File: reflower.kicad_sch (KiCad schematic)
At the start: 37 parts, among them J1 Jack-DC, SW1 RotaryEncoder_Switch, U1 AT32UC3B0256, U2 NCP1117-3.3, U3 MAX31855KASA

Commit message: readme
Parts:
- LOAD1: value (none) -> Conn_01x02; footprint (none) -> Connector_PinHeader_2.54mm:PinHeader_1x06_P2.54mm_Vertical
- SCREEN1: value (none) -> Conn_01x12
- SDCARD1: value (none) -> Conn_01x06
- U4: value (none) -> CPC40055ST; footprint (none) -> OptoDevice:Finder_34.81
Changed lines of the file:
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@@
 (kicad_sch (version 20211123) (generator eeschema)
   (paper "A4")
+  (bus_alias "SPI" (members "SCLK" "MOSI" "MISO"))
   (bus_alias "SCREEN" (members "SC_CS" "BL" "DC" "RES" "T_SDA" "T_SCL" "T_INT"))
-  (bus_alias "SPI" (members "SCLK" "MOSI" "MISO"))
   (junction (at 66.294 144.272) (diameter 0) (color 0 0 0 0)
   )
@@
       (effects (font (size 1.27 1.27)) hide)
     )
-    (property "Value" "" (id 1) (at 173.609 139.192 0))
+    (property "Value" "GND" (id 1) (at 173.609 139.192 0))
     (property "Footprint" "" (id 2) (at 176.784 139.192 0)
       (effects (font (size 1.27 1.27)) hide)
@@
       (effects (font (size 1.27 1.27)) (justify right))
     )
-    (property "Value" "" (id 1) (at 253.365 76.835 0)
+    (property "Value" "Conn_01x12" (id 1) (at 253.365 76.835 0)
       (effects (font (size 1.27 1.27)) (justify right))
     )
@@
       (effects (font (size 1.27 1.27)) (justify right))
     )
-    (property "Value" "" (id 1) (at 253.365 146.05 0)
+    (property "Value" "Conn_01x02" (id 1) (at 253.365 146.05 0)
       (effects (font (size 1.27 1.27)) (justify right))
     )
-    (property "Footprint" "" (id 2) (at 254.635 152.4 0)
+    (property "Footprint" "Connector_PinHeader_2.54mm:PinHeader_1x06_P2.54mm_Vertical" (id 2) (at 254.635 152.4 0)
       (effects (font (size 1.27 1.27)) hide)
     )
@@
     (in_bom yes) (on_board yes)
     (property "Reference" "U4" (id 0) (at 184.404 141.732 0))
-    (property "Value" "" (id 1) (at 184.404 144.272 0))
-    (property "Footprint" "" (id 2) (at 179.324 141.732 0)
+    (property "Value" "CPC40055ST" (id 1) (at 184.404 144.272 0))
+    (property "Footprint" "OptoDevice:Finder_34.81" (id 2) (at 179.324 141.732 0)
       (effects (font (size 1.27 1.27) italic) (justify left) hide)
     )
@@
       (effects (font (size 1.27 1.27)) (justify right))
     )
-    (property "Value" "" (id 1) (at 253.365 117.475 0)
+    (property "Value" "Conn_01x06" (id 1) (at 253.365 117.475 0)
       (effects (font (size 1.27 1.27)) (justify right))
     )

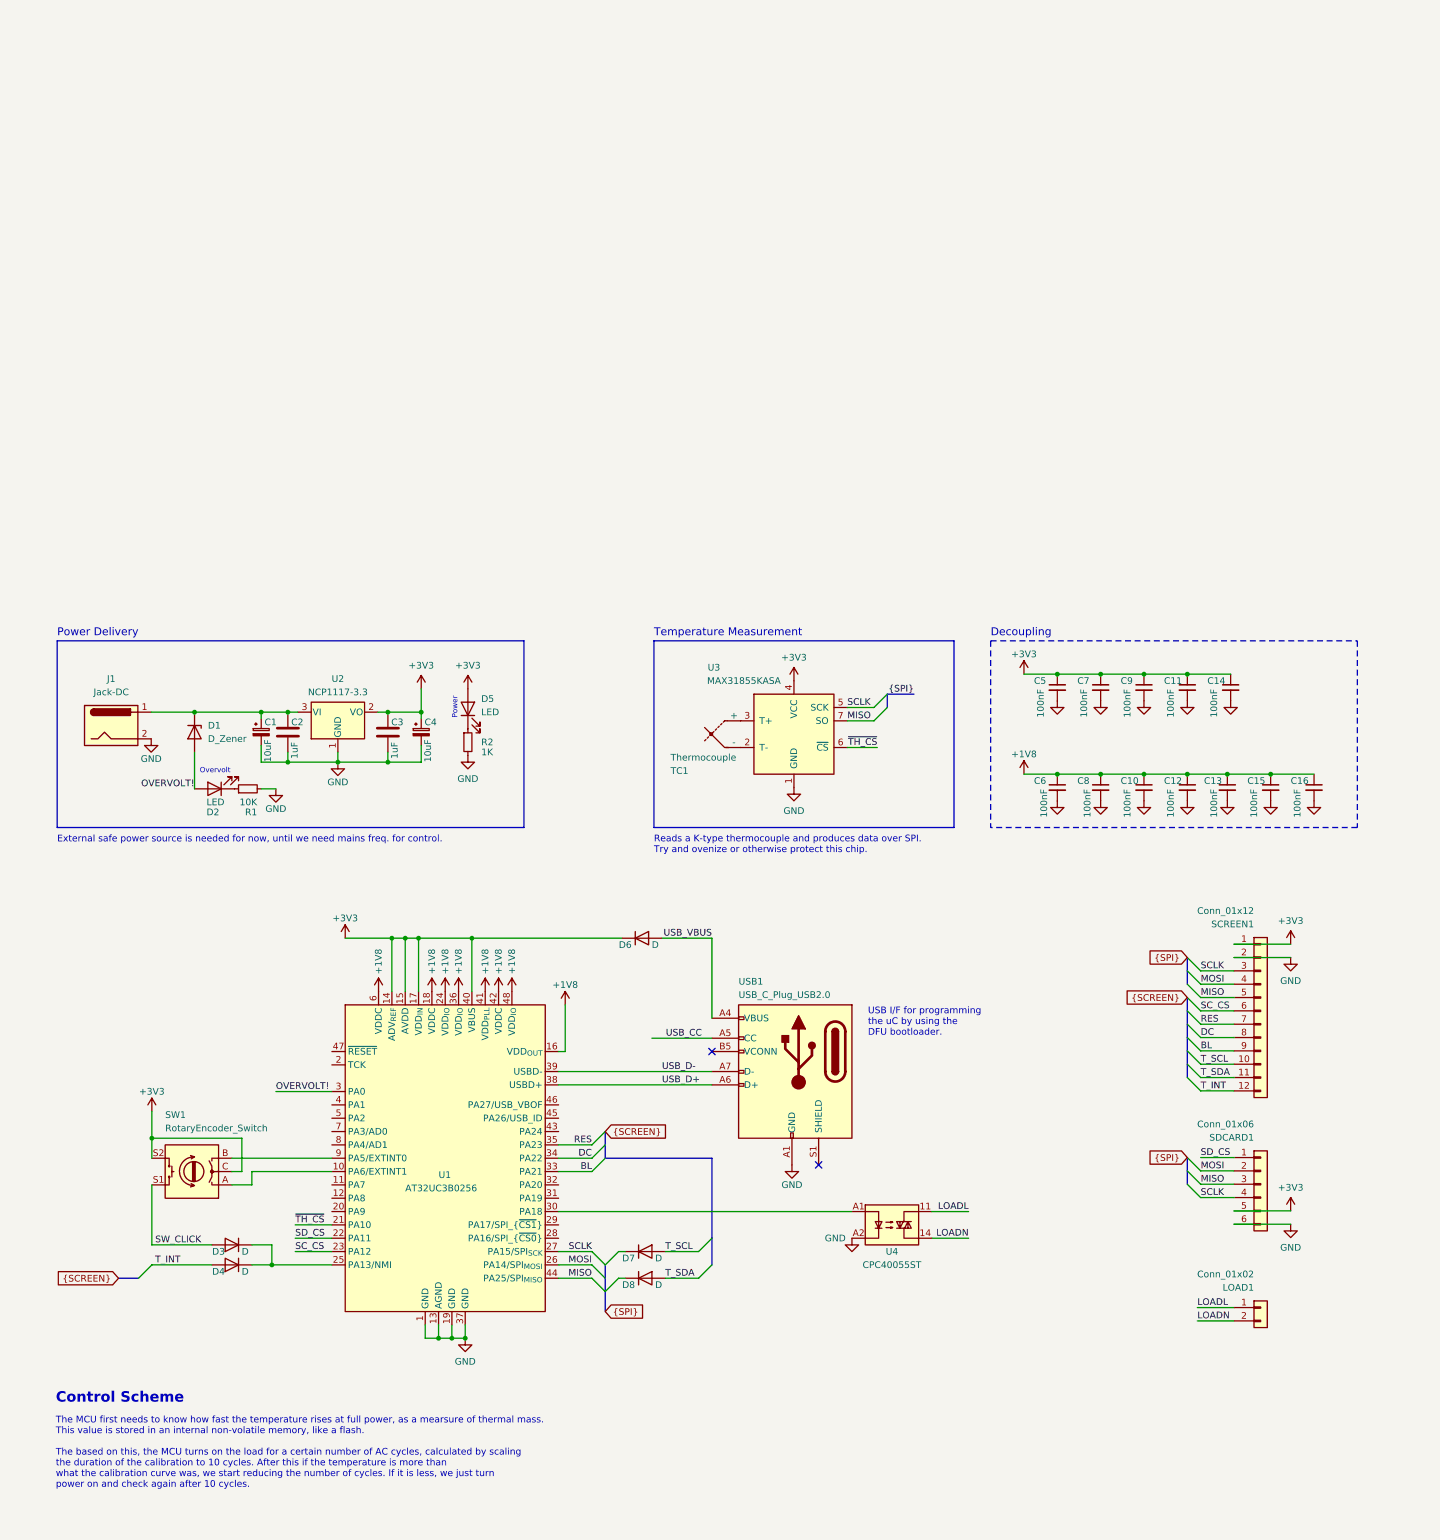
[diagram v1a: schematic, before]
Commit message: added separate SD card slot
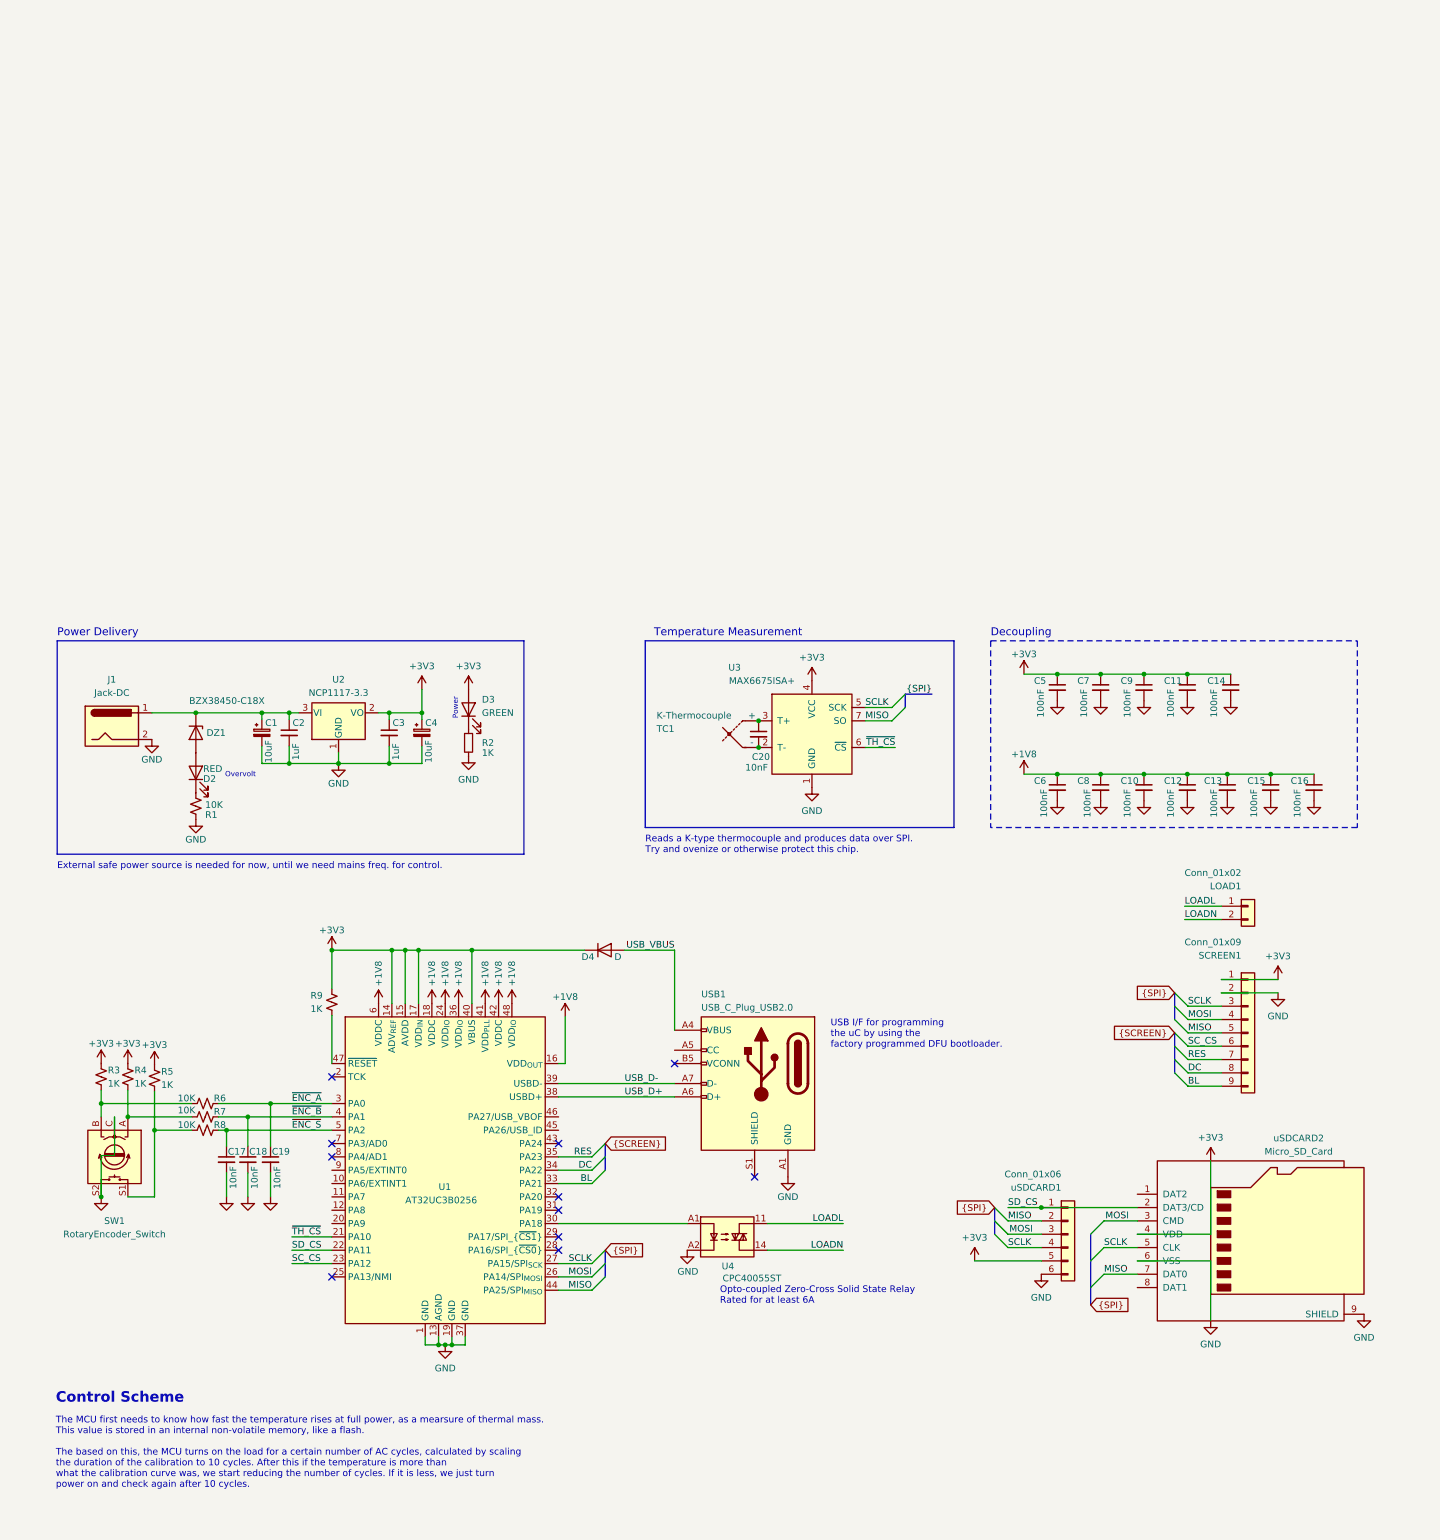
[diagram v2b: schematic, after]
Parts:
- removed D3, D4, D7, D8: D, symbol Device:D
- added C17, C18, C19, C20: 10nF, Capacitor_SMD:C_0603_1608Metric, symbol Device:C_Small
- added R3, R4, R5, R9: 1K, Resistor_SMD:R_0603_1608Metric, symbol Device:R_Small_US
- added R6, R7, R8: 10K, Resistor_SMD:R_0603_1608Metric, symbol Device:R_Small_US
- added uSDCARD2: Micro_SD_Card, symbol Connector:Micro_SD_Card
- C1, C10, C11, C12, C13, C14, C15, C16, C4, C5, C6, C7, C8, C9: footprint (none) -> Capacitor_SMD:C_0603_1608Metric
- C2, C3: footprint (none) -> Capacitor_SMD:C_0603_1608Metric; symbol Device:C -> Device:C_Small
- D2: value LED -> RED
- D3: renamed from D5; value LED -> GREEN
- DZ1: renamed from D1; value D_Zener -> BZX38450-C18X; footprint (none) -> Diode_SMD:D_SOD-323
- R1: footprint (none) -> Resistor_SMD:R_0603_1608Metric; symbol Device:R_Small -> Device:R_Small_US
- R2: footprint (none) -> Resistor_SMD:R_0603_1608Metric
- SCREEN1: value Conn_01x12 -> Conn_01x09; symbol Connector_Generic:Conn_01x12 -> Connector_Generic:Conn_01x09
- TC1: value Thermocouple -> K-Thermocouple; footprint (none) -> Connector_PinHeader_2.54mm:PinHeader_1x02_P2.54mm_Vertical
- U3: value MAX31855KASA -> MAX6675ISA+
- renumbered D6 to D4, SDCARD1 to uSDCARD1
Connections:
- net +3V3: now also R3.1, R4.1, R5.1, R9.1, uSDCARD2.4 (VDD); no longer SW1.C, SW1.S2
- net GND: now also SW1.C, SW1.S2, C17.2, C18.2, C19.2, uSDCARD2.6 (VSS), uSDCARD2.9 (SHIELD)
- net MISO: now also uSDCARD1.2 (Pin_2), uSDCARD2.7 (DAT0); no longer uSDCARD1.3 (Pin_3)
- net MOSI: now also uSDCARD1.3 (Pin_3), uSDCARD2.3 (CMD); no longer uSDCARD1.2 (Pin_2)
- net SCLK: now also uSDCARD2.5 (CLK)
- net SD_CS: now also uSDCARD2.2 (DAT3/CD)
- net at U1.10 (PA6/EXTINT1): no longer SW1.A
- net ~{ENC_B}: now reaches U1.4 (PA1)
- net ~{ENC_B}: now also C18.1, R7.2
- net at U1.47 (~{RESET}): now also R9.2
- net ~{ENC_S}: now reaches U1.5 (PA2)
- net ~{ENC_S}: now also C17.1, R8.2
- net at U1.9 (PA5/EXTINT0): no longer SW1.B
- net at TC1.2 (-), U3.2 (T-): now also C20.2
- net at TC1.1 (+), U3.3 (T+): now also C20.1
- net OVERVOLT!: no longer names the net of D2.2 (A), DZ1.2 (A)
- net OVERVOLT!: no longer U1.3 (PA0)
- net SW_CLICK: no longer names the net of SW1.S1
- net SW_CLICK: now also R5.2, R8.1
- removed net T_INT: SCREEN1.12 (Pin_12)
- removed net T_SCL: SCREEN1.10 (Pin_10)
- removed net T_SDA: SCREEN1.11 (Pin_11)
- net USB_CC: no longer names the net of USB1.A5 (CC)
- new net: R4.2, R7.1, SW1.A
- new net: R3.2, R6.1, SW1.B
- new net ~{ENC_A}: C19.1, R6.2, U1.3 (PA0)
- no-connect marks 2 -> 11
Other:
- note added: "Opto-coupled Zero-Cross Solid State Relay Rated for at least 6A"
- note added: "USB I/F for programming the uC by using the factory programmed DFU bootloader."
- note removed: "USB I/F for programming the uC by using the DFU bootloader."
- moved on the sheet: D2, D4, LOAD1, SW1, TC1, U1, U3, U4, uSDCARD1

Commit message: schematic improvements
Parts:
- added R10, R11: 10K, Resistor_SMD:R_0603_1608Metric, symbol Device:R_Small_US
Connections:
- net GND: now also R10.1, R11.1
- net at USB1.A5 (CC): now also R10.2, R11.2
- no-connect marks 11 -> 20
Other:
- moved on the sheet: C1, C2, C3, C4, D2, DZ1, J1, LOAD1, R1, SCREEN1, U2

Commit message: routing start
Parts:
- removed uSDCARD1: Conn_01x06, Connector_PinHeader_2.54mm:PinHeader_1x06_P2.54mm_Vertical, symbol Connector_Generic:Conn_01x06
- C1, C4: value 10uF -> (none); footprint Capacitor_SMD:C_0603_1608Metric -> (none)
- C2, C3: value 1uF -> (none); footprint Capacitor_SMD:C_0603_1608Metric -> (none); symbol Device:C_Small -> Device:C_Polarized_Small
- D2: footprint (none) -> LED_THT:LED_D3.0mm
- D3: footprint (none) -> LED_THT:LED_D3.0mm_Clear
- D4: footprint (none) -> Diode_SMD:D_0603_1608Metric
- J1: footprint (none) -> TerminalBlock_Phoenix:TerminalBlock_Phoenix_MKDS-1,5-2_1x02_P5.00mm_Horizontal
- LOAD1: value Conn_01x02 -> Conn_01x03; footprint Connector_PinHeader_2.54mm:PinHeader_1x06_P2.54mm_Vertical -> TerminalBlock_Phoenix:TerminalBlock_Phoenix_MKDS-1,5-3_1x03_P5.00mm_Horizontal; symbol Connector_Generic:Conn_01x02 -> Connector_Generic:Conn_01x03
- R2: symbol Device:R_Small -> Device:R_Small_US
- RELAY1: renamed from U4; footprint OptoDevice:Finder_34.81 -> SolidStateRelay:IXYS CPC40055ST
- SCREEN1: footprint Connector_PinHeader_2.54mm:PinHeader_1x12_P2.54mm_Vertical -> Connector_PinHeader_2.54mm:PinHeader_1x09_P2.54mm_Horizontal
- TC1: footprint Connector_PinHeader_2.54mm:PinHeader_1x02_P2.54mm_Vertical -> TerminalBlock_Phoenix:TerminalBlock_Phoenix_MKDS-1,5-2_1x02_P5.00mm_Horizontal
- uSDCARD1: renamed from uSDCARD2; footprint (none) -> Connector_Card:microSD_HC_Molex_104031-0811
- renumbered R4 to R3, R3 to R4, R7 to R6, R6 to R7
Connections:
- net GND: now also RELAY1.4; no longer RELAY1.A2
- net LOADL: now also RELAY1.1; no longer RELAY1.11
- net LOADN: now also LOAD1.3 (Pin_3), RELAY1.2; no longer LOAD1.2 (Pin_2), RELAY1.14
- net ~{ENC_A}: now also C18.1, R6.2, U1.4 (PA1); no longer C19.1, R7.2, U1.3 (PA0)
- net ~{ENC_B}: now also C19.1, R7.2, U1.3 (PA0); no longer C18.1, R6.2, U1.4 (PA1)
- net at U1.30 (PA18): now also RELAY1.3; no longer RELAY1.A1
- net PWR: now reaches C1.1, C2.1, DZ1.1 (K), J1.1, U2.3 (VI)
- no-connect marks 20 -> 21
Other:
- company: (none) -> zrthxn
- title: (none) -> Reflow Controller
- moved on the sheet: C17, C18, C19, uSDCARD1
